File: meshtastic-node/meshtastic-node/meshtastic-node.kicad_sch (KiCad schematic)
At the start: 62 parts, among them IC1 CH224K, IC2 CN3791, IC3 SKY65313-21, IC4 AS169-73LF, IC5 Wio-WM1110, IC6 INA220AIDGSR, J1 USB_C_Receptacle_USB2.0, J2 Conn_01x05_Socket, J4 Conn_01x02_Socket, J5 Conn_01x02_Socket, J6 Conn_ARM_JTAG_SWD_10, Q1 PMOS, U1 TPS565208, U2 TPS61222DCK, U3 TPS61022

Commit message: Meshtastic
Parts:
- removed IC4: AS169-73LF, SOT95P270X145-6N, symbol AS169-73LF:AS169-73LF
- removed U3: TPS61022, Package_DFN_QFN:Texas_RWU0007A_VQFN-7_2x2mm_P0.5mm, symbol Converter_DCDC:TPS61022
- added AE1, AE3: Antenna_Shield, symbol Device:Antenna_Shield
- added C22, C23: 100nF, symbol Device:C
- added C25, C30: 220pF, symbol Device:C
- added C26, C29: 470pF, symbol Device:C
- added C27: 4700pF, symbol Device:C
- added C28: 0.047uF, symbol Device:C
- added C31, C32, C33: 1.0pF, symbol Device:C
- added C34, C35: 10uF, Capacitor_SMD:C_0805_2012Metric_Pad1.18x1.45mm_HandSolder, symbol Device:C
- added C38, C39: 22uF, Capacitor_SMD:C_0805_2012Metric_Pad1.18x1.45mm_HandSolder, symbol Device:C
- added IC7: XA2163, SON50P150X150X40-7N, symbol XA2163:XA2163
- added L6: 3.9nH, Inductor_SMD:L_0805_2012Metric_Pad1.15x1.40mm_HandSolder, symbol Device:L
- added L7, L8: 4.7nH, Inductor_SMD:L_0805_2012Metric_Pad1.15x1.40mm_HandSolder, symbol Device:L
- added L9: 4.7uH, Inductor_SMD:L_0805_2012Metric_Pad1.15x1.40mm_HandSolder, symbol Device:L
- added R16, R17, R18, R19: 4.7k, symbol Device:R
- added R20: 100k, symbol Device:R
- added R21: 700k, symbol Device:R
- added SW2: SW_Push, symbol Switch:SW_Push
- added SW3: SW_DPDT_x2, symbol Switch:SW_DPDT_x2
- added U3: TPS61222DCK, Package_TO_SOT_SMD:Texas_R-PDSO-G6, symbol Regulator_Switching:TPS61222DCK
- added U4: BME280, Package_LGA:Bosch_LGA-8_2.5x2.5mm_P0.65mm_ClockwisePinNumbering, symbol Sensor:BME280
- added U5: INA3221, Package_DFN_QFN:Texas_RGV0016A_VQFN-16-1EP_4x4mm_P0.65mm_EP2.1x2.1mm, symbol Power_Management:INA3221
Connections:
- net +3V3: now also IC3.16 (VDD1), IC3.17 (VCC_RX), IC3.3 (CTL2), IC3.5 (VPC), IC6.1 (A1), C22.2, C23.2, C29.1, C30.1, C34.1, L9.1, R16.2, R17.1, SW3.2 (B), U3.1 (VIN), U3.6 (EN), U4.2 (CSB), U4.5 (SDO), U4.6 (VDDIO), U4.8 (VDD)
- net +4V: now also IC3.23 (VDD2), IC3.24 (VCC_TX1), IC3.25 (VCC_TX2), IC3.26 (VCC_TX3), C25.1, C26.1, C27.1, C28.1
- net +5V: now also C21.1, C21.2, IC6.10 (VIN+), IC6.9 (VIN-), R14.1, R15.2, C35.1, C38.1, C39.1, R21.1, U3.4 (VOUT)
- net Bat+: no longer C17.1, IC2.7 (BAT), R8.2
- net GND: now also AE2.2 (Shield), IC3.1 (GND_1), IC3.11 (GND_5), IC3.12 (GND_6), IC3.14 (GND_7), IC3.15 (GND_8), IC3.19 (GND_9), IC3.21 (GND_10), IC3.22 (GND_11), IC3.27 (GND_12), IC3.28 (GND_13), IC3.29 (GND_14), IC3.30 (GND_15), IC3.31 (GND_16), IC3.32 (GND_17), IC3.33 (GND_18), IC3.34 (GND_19), IC3.35 (GND_20), IC3.36 (GND_21), IC3.37 (GND_22), IC3.38 (GND_23), IC3.39 (GND_24), IC3.4 (CTL3), IC3.40 (GND_25), IC3.41 (GND_26), IC3.42 (GND_27), IC3.43 (GND_28), IC3.44 (GND_29), IC3.6 (GND_2), IC3.8 (GND_3), IC3.9 (GND_4), IC6.2 (A0), AE1.2 (Shield), AE3.2 (Shield), C22.1, C23.1, C25.2, C26.2, C27.2, C28.2, C29.2, C30.2, C31.2, C32.2, C33.2, C34.2, C35.2, C38.2, C39.2, IC7.1 (GND_1), IC7.7 (GND_2), R18.1, R19.1, R20.2, U3.3 (GND), U4.1 (GND), U4.7 (GND); no longer IC6.1 (A1)
- net I2C SCL: now also R17.2, U4.4 (SCK); no longer IC6.2 (A0)
- net I2C SDA: now also R16.1, U4.3 (SDI)
- net at AE2.1 (A): now also IC3.7 (ANT)
- net RF_WIFI_BT: now reaches IC5.63 (ANT_NRF)
- net RF_WIFI_BT: now also L6.1
- net at IC3.18 (RX3), IC3.20 (TX): now also IC7.3 (OUT2(RX))
- net at IC3.10 (RX1): now also IC3.13 (RX2)
- net RADIO TX/RX: now reaches IC3.2 (CTL1)
- net BatIn+ renamed BatLoad+
- net BatLoad+: now also C17.1, IC2.7 (BAT), R8.2
- net RF_LORA_SIG renamed RF_LORA
- net RF_LORA: now also IC7.6 (IN(ANT))
- new net: AE1.1 (A), C33.1, L8.2
- new net: C32.1, IC7.4 (OUT1(TX)), L8.1
- new net: R20.1, R21.2, U3.2 (FB)
- new net: L9.2, U3.5 (L)
- new net: C31.1, L6.2, L7.1
- new net: AE3.1 (A), L7.2
- new net USE_ANT_1: IC7.5 (VCONT1), R19.2, SW3.1 (A)
- new net USE_ANT_2: IC7.2 (VCONT2), R18.2, SW3.3 (C)
- no-connect marks 4 -> 6
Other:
- note added: "I2C ADDR 0x40"
- note added: "I2C ADDR 0x77"
- note added: "SWD / JTAG"
- note added: "USB"
- note removed: "ACCEL / GYRO / COMPASS"
- note removed: "I2C ADDR 0xF424B"
- note removed: "SWD"
- note removed: "USB-C"
- moved on the sheet: AE2, C1, C17, C18, C19, C2, C20, C21, C3, C4, C5, C6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

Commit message: Swap switch
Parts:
- removed AE2: Antenna_Shield, Connector_Coaxial:SMA_Molex_73251-2120_EdgeMount_Horizontal, symbol Device:Antenna_Shield
- removed IC7: XA2163, SON50P150X150X40-7N, symbol XA2163:XA2163
- removed R18: 4.7k, symbol Device:R
- added C36: 100pF, symbol Device:C
- added J3: Conn_Coaxial_Small, symbol Connector:Conn_Coaxial_Small
- added R22: 4.7k, symbol Device:R
- added S1: HMC544AETR, SOT95P280X145-6N, symbol HMC544AETR:HMC544AETR
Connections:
- net GND: now also J3.2 (Ext), R22.2, S1.2 (GND)
- net RF_LORA: now also C36.1
- net USE_ANT_1: now also R22.1, S1.6 (A); no longer R19.2
- net USE_ANT_2: now also R19.2, S1.4 (B)
- net at IC3.7 (ANT): now also J3.1 (In)
- net at C32.1, L8.1: now also S1.1 (RF2)
- net at IC3.18 (RX3), IC3.20 (TX): now also S1.3 (RF1)
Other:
- moved on the sheet: AE1, AE3, C25, C26, C27, C28, C29, C30, C31, C32, C33, IC3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

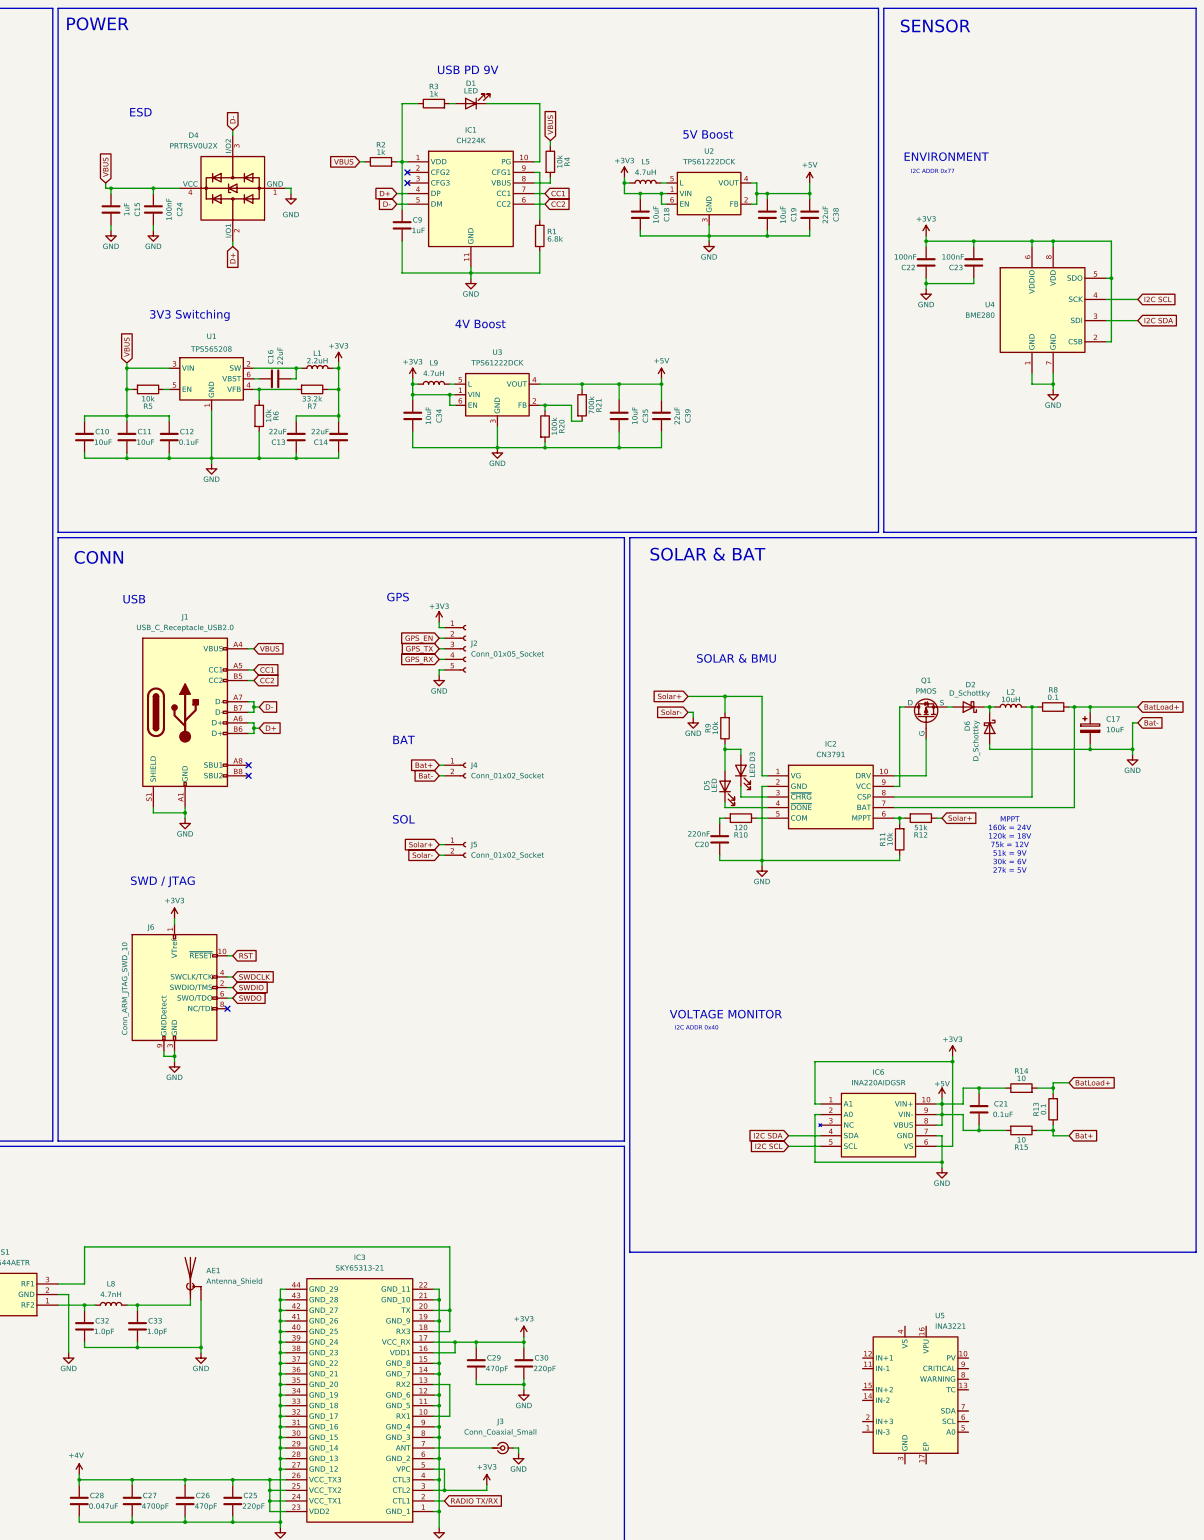
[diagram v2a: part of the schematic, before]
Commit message: power switching
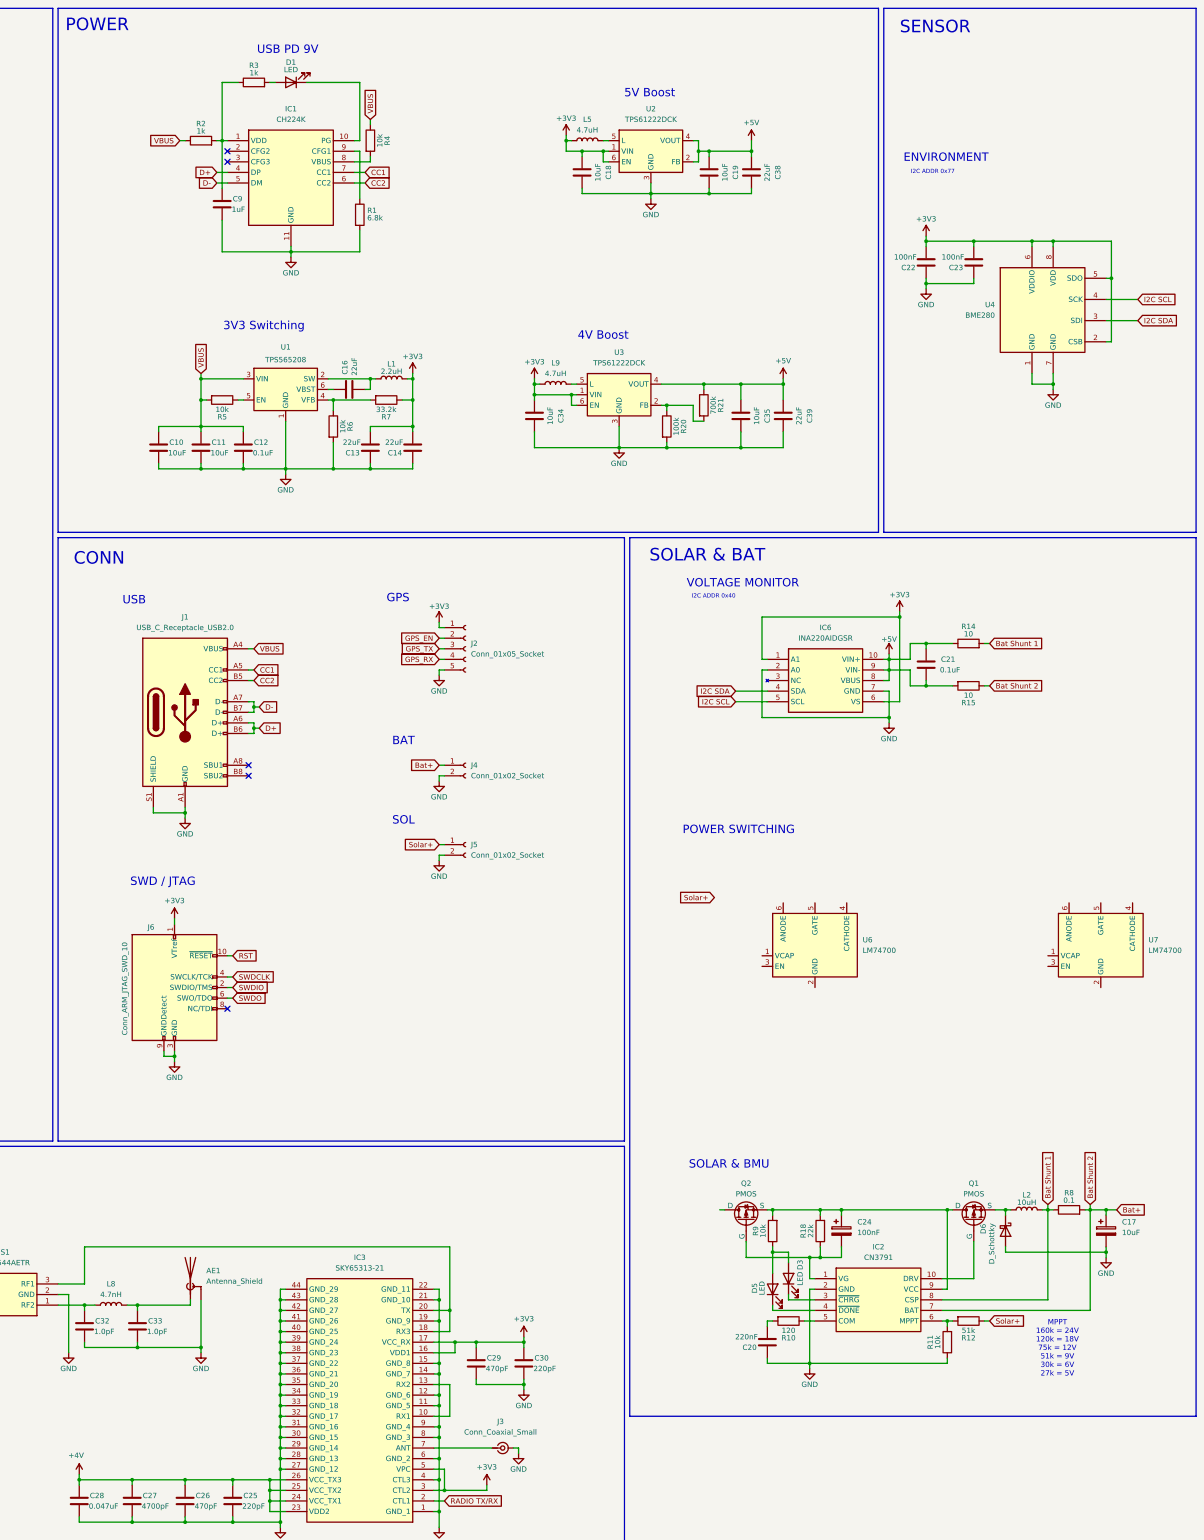
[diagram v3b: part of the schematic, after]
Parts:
- removed C15: 1uF, Capacitor_SMD:C_0805_2012Metric_Pad1.18x1.45mm_HandSolder, symbol Device:C
- removed C24: 100nF, Capacitor_SMD:C_0805_2012Metric_Pad1.18x1.45mm_HandSolder, symbol Device:C
- removed D2: D_Schottky, symbol Device:D_Schottky
- removed D4: PRTR5V0U2X, Package_TO_SOT_SMD:SOT-143, symbol Power_Protection:PRTR5V0U2X
- removed R13: 0.1, symbol Device:R
- removed U5: INA3221, Package_DFN_QFN:Texas_RGV0016A_VQFN-16-1EP_4x4mm_P0.65mm_EP2.1x2.1mm, symbol Power_Management:INA3221
- added C24: 100nF, symbol Device:C_Polarized
- added Q2: PMOS, symbol Simulation_SPICE:PMOS
- added R18: 22k, symbol Device:R
- added U6, U7: LM74700, Package_TO_SOT_SMD:SOT-23-6, symbol Power_Management:LM74700
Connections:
- net Solar+: no longer IC2.1 (VG), R9.2
- net at D6.1 (K), L2.1: now also Q1.3 (S)
- net Bat Shunt 1: now reaches IC2.8 (CSP), L2.2, R8.1
- net Bat Shunt 1: now also R14.2
- net at IC2.9 (VCC), Q1.1 (D): now also R9.2, C24.1, Q2.3 (S), R18.2
- net Bat+ renamed Bat Shunt 2
- net Bat Shunt 2: now also C17.1, IC2.7 (BAT), R8.2
- removed net BatLoad+: C17.1, IC2.7 (BAT), R14.2, R8.2
- new net: C24.2, IC2.1 (VG), Q2.2 (G), R18.1
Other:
- note added: "POWER SWITCHING"
- note removed: "ESD"
- moved on the sheet: C10, C11, C12, C13, C14, C16, C17, C18, C19, C20, C21, C34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

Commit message: changes
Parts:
- removed C21: 0.1uF, symbol Device:C
- removed C32, C33: 1.0pF, symbol Device:C
- removed IC6: INA220AIDGSR, SOP50P490X110-10N, symbol INA220AIDGSR:INA220AIDGSR
- removed L8: 4.7nH, Inductor_SMD:L_0805_2012Metric_Pad1.15x1.40mm_HandSolder, symbol Device:L
- removed R15: 10, symbol Device:R
- removed U6, U7: LM74700, Package_TO_SOT_SMD:SOT-23-6, symbol Power_Management:LM74700
- added C37, C40: 1uF, Capacitor_SMD:C_0805_2012Metric_Pad1.18x1.45mm_HandSolder, symbol Device:C
- added D2: LED, LED_SMD:LED_0805_2012Metric_Pad1.15x1.40mm_HandSolder, symbol Device:LED
- added IC4, IC7: TPS2121RUXT, TPS2121RUXT, symbol TPS2121RUXT:TPS2121RUXT
- added R13, R23: 51.1k, Resistor_SMD:R_0805_2012Metric_Pad1.20x1.40mm_HandSolder, symbol Device:R
- added R24: 4.7k, Resistor_SMD:R_0805_2012Metric_Pad1.20x1.40mm_HandSolder, symbol Device:R
- added R25, R29, R31, R32: 5k, Resistor_SMD:R_0805_2012Metric_Pad1.20x1.40mm_HandSolder, symbol Device:R
- added R26, R27, R28, R30: 23.7k, Resistor_SMD:R_0805_2012Metric_Pad1.20x1.40mm_HandSolder, symbol Device:R
- added R36, R37, R38: 0.1, Resistor_SMD:R_0805_2012Metric_Pad1.20x1.40mm_HandSolder, symbol Device:R
- added TP1, TP2, TP3, TP4, TP5, TP6: TestPoint, TestPoint:TestPoint_Pad_D2.0mm, symbol Connector:TestPoint
- added U5: INA3221, Package_DFN_QFN:Texas_RGV0016A_VQFN-16-1EP_4x4mm_P0.65mm_EP2.1x2.1mm, symbol Power_Management:INA3221
- AE3: footprint (none) -> RF_Antenna:Texas_SWRA117D_2.4GHz_Right
- C1, C10, C11, C12, C13, C14, C16, C2, C20, C22, C23, C25, C26, C27, C28, C29, C3, C30, C31, C36, C4, C5, C6, C7, C8, C9: footprint (none) -> Capacitor_SMD:C_0805_2012Metric_Pad1.18x1.45mm_HandSolder
- D1, D3, D5: footprint (none) -> LED_SMD:LED_0805_2012Metric_Pad1.15x1.40mm_HandSolder
- J2: footprint (none) -> Connector_JST:JST_EH_S5B-EH_1x05_P2.50mm_Horizontal
- J3: footprint (none) -> Connector_Coaxial:SMA_Molex_73251-1153_EdgeMount_Horizontal
- J4, J5: footprint (none) -> Connector_JST:JST_EH_S2B-EH_1x02_P2.50mm_Horizontal
- J6: footprint (none) -> Connector_PinHeader_1.27mm:PinHeader_2x05_P1.27mm_Vertical
- L1: footprint (none) -> Inductor_SMD_Wurth:L_Wurth_WE-LQSH-4020
- L2: footprint (none) -> Inductor_SMD:L_0805_2012Metric_Pad1.15x1.40mm_HandSolder
- Q1, Q2: footprint (none) -> Package_TO_SOT_SMD:SOT-23_Handsoldering
- R1, R10, R11, R12, R16, R17, R18, R19, R2, R20, R21, R22, R3, R4, R5, R6, R7, R8, R9: footprint (none) -> Resistor_SMD:R_0805_2012Metric_Pad1.20x1.40mm_HandSolder
- R14: value 10 -> 1k; footprint (none) -> Resistor_SMD:R_0805_2012Metric_Pad1.20x1.40mm_HandSolder
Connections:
- net Bat Shunt 2 is gone; now on net Bat Shunt 1: C17.1, IC2.7 (BAT), J4.1 (Pin_1), R8.2
- net +3V3: now also R4.1, R24.1, U5.16 (VPU), U5.4 (VS)
- net +5V: no longer R14.1
- net Bat Shunt 1: now also IC7.2 (IN2), R27.1, R36.2, U5.11 (IN-1), U5.12 (IN+1); no longer IC2.8 (CSP), L2.2, R14.2
- net D+: now also IC5.41 (DP)
- net D-: now also IC5.40 (DN)
- net GND: now also SW2.1, C37.2, C40.2, D2.1 (K), IC4.12 (GND), IC4.3 (CP2), IC4.6 (PR1), IC4.9 (ST), IC7.12 (GND), IC7.6 (PR1), IC7.9 (ST), R13.2, R23.2, R25.2, R29.2, R31.2, R32.2, U5.3 (GND)
- net GPS_EN: now also IC5.47 (P0.24)
- net GPS_RX: now also IC5.45 (P0.20)
- net GPS_TX: now also IC5.46 (P0.22)
- net I2C SCL: now also IC5.57 (P1.05), TP1.1, U5.6 (SCL)
- net I2C SDA: now also IC5.58 (P1.04), TP2.1, U5.7 (SDA)
- net RADIO TX/RX: now also IC5.54 (P1.01), TP6.1
- net SWDCLK: now also IC5.51 (SWDCLK)
- net SWDIO: now also IC5.50 (SWDIO)
- net VBUS: now also IC4.7 (IN1), IC7.7 (IN1), R28.1, R30.1, TP3.1; no longer C10.1, C11.1, C12.1, R4.1, R5.2, U1.3 (VIN)
- net at AE1.1 (A): now also S1.1 (RF2)
- net Charger Load: now reaches Q2.1 (D)
- net Charger Load: now also R12.1, IC4.1 (OUT_1), IC4.8 (OUT_2)
- net at S1.5 (RFC): now also C36.2
- net at IC5.13 (P0.03): now also R14.2
- net USR_BUTTON: now reaches IC5.48 (P1.00)
- net USR_BUTTON: now also SW2.2, R24.2
- net SWDO: no longer names the net of J6.6 (SWO/TDO)
- net Solar+ renamed Sol Shunt 1
- net Sol Shunt 1: now also IC4.2 (IN2), R26.1, R37.1, R37.2, TP4.1, U5.14 (IN-2), U5.15 (IN+2); no longer R12.1
- new net: IC7.5 (OV1), R30.2, R31.1
- new net: IC7.4 (OV2), R27.2, R32.1
- new net: IC2.8 (CSP), L2.2, R36.1
- new net: D2.2 (A), R14.1
- new net: C40.1, IC7.11 (SS)
- new net: IC7.10 (ILIM), R23.1
- new net: IC4.4 (OV2), R25.1, R26.2
- new net: IC4.5 (OV1), R28.2, R29.1
- new net: IC4.10 (ILIM), R13.1
- new net: C37.1, IC4.11 (SS)
- new net Sys Load: C10.1, C11.1, C12.1, IC7.1 (OUT_1), IC7.8 (OUT_2), R38.1, R38.2, R5.2, TP5.1, U1.3 (VIN), U5.1 (IN-3), U5.2 (IN+3)
- no-connect marks 6 -> 47
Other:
- note added: "I2C ADDR 0x42"
- note added: "MPPT 120k = 18V 75k = 12V 51k = 9V 30k = 6V 27k = 5V"
- note removed: "I2C ADDR 0x40"
- note removed: "MPPT 160k = 24V 120k = 18V 75k = 12V 51k = 9V 30k = 6V 27k = 5V"
- moved on the sheet: AE1, AE3, C17, C20, C24, C31, D3, D5, D6, IC2, L2, L6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
